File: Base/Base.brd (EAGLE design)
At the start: 83.8 x 61 mm, 25 parts

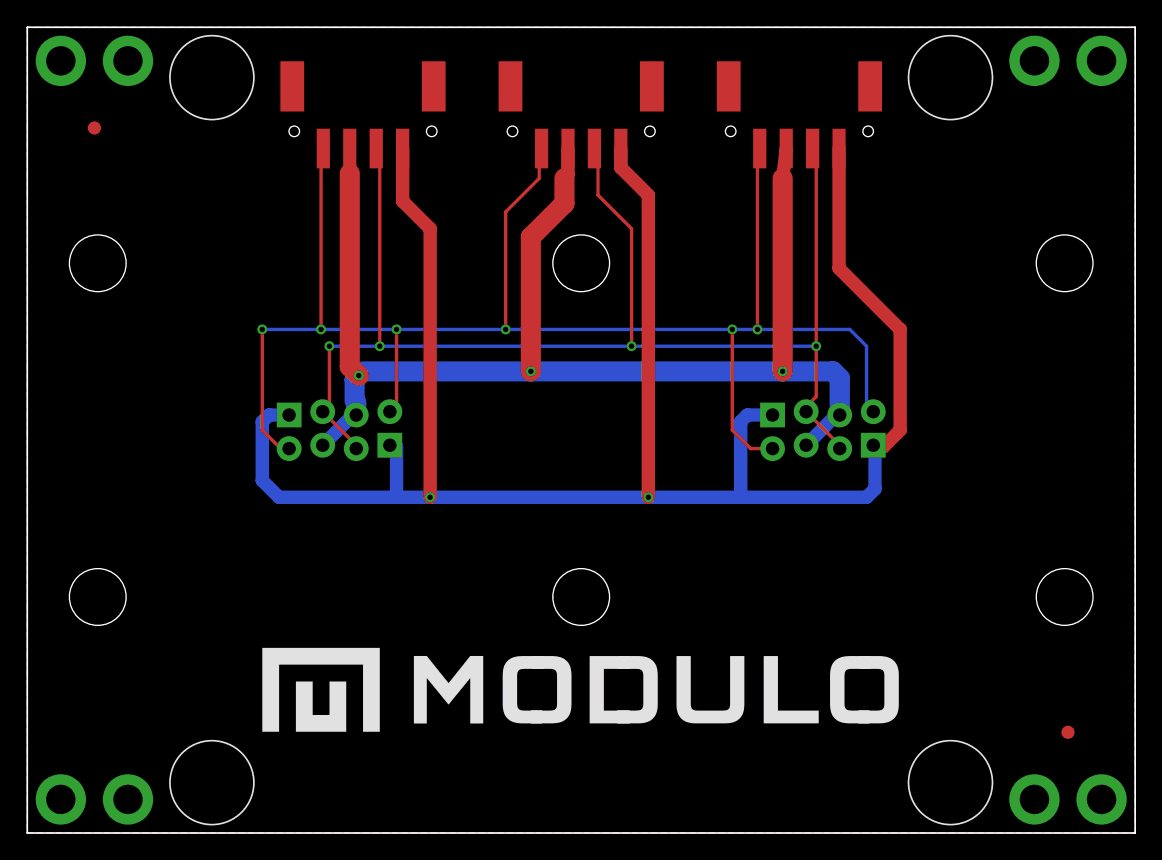
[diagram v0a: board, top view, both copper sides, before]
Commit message: Check point of current PCB designs. Among other things I think this change includes rewiring of programming lines on many of the boards,.
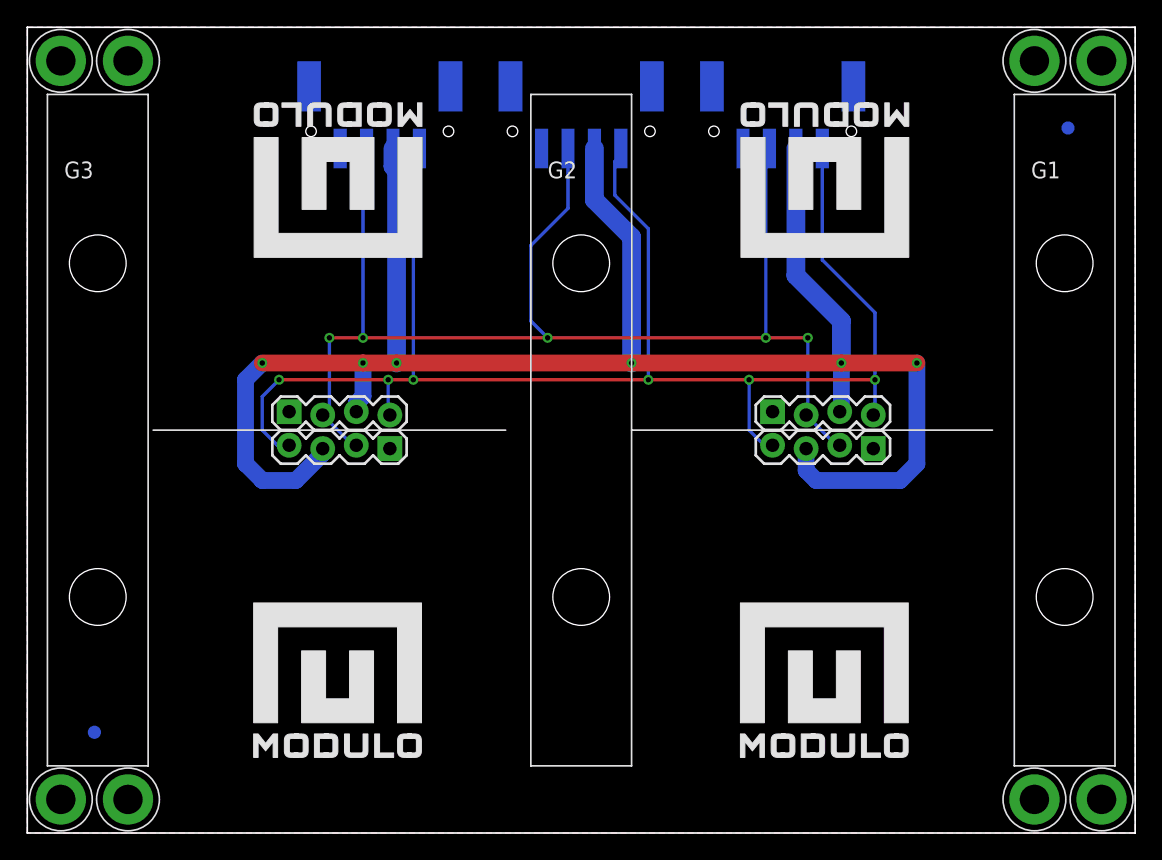
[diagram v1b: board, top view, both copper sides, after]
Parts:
- moved H1 78.7 mm to (2.54, 58.4), flipped to the top
- moved H5 78.7 mm to (2.54, 2.54), flipped to the top
- moved H6 78.7 mm to (81.3, 2.54), flipped to the top
- moved H8 78.7 mm to (81.3, 58.4), flipped to the top
- moved F1 73.7 mm to (5.08, 7.62), flipped to the bottom
- moved F2 73.7 mm to (78.7, 53.3), flipped to the bottom
- moved G1 73.2 mm to (78.5, 30.5), flipped to the top
- moved G3 73.2 mm to (5.33, 30.5), flipped to the top
- moved H2 68.6 mm to (7.62, 2.54), flipped to the top
- moved H3 68.6 mm to (76.2, 58.4), flipped to the top
- moved H4 68.6 mm to (76.2, 2.54), flipped to the top
- moved H7 68.6 mm to (7.62, 58.4), flipped to the top
- moved U$1 47.6 mm to (65.4, 12.1), flipped to the bottom
- moved JP1 44.3 mm to (19.8, 31.8), flipped to the top
- moved JP6 44.3 mm to (64.0, 29.2), flipped to the top
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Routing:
- net GND: track 150.2 -> 0.00 mm, vias 2 -> 0
- net VCC: track 102.0 -> 142.8 mm, vias 3 -> 6
- net SCL: track 124.9 -> 119.0 mm
- net SDA: track 104.9 -> 100.2 mm, vias 4 -> 5

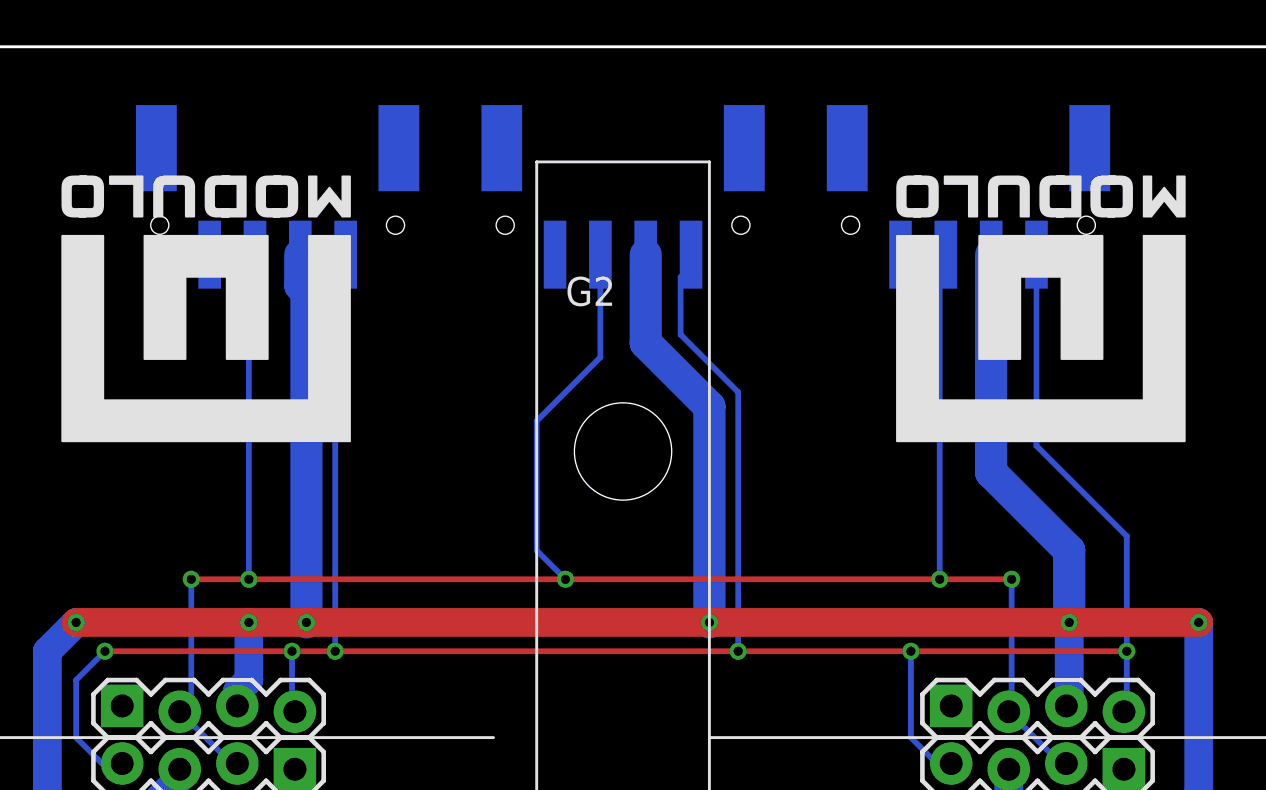
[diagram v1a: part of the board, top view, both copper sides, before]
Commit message: Updated to grove compatible connector footprints
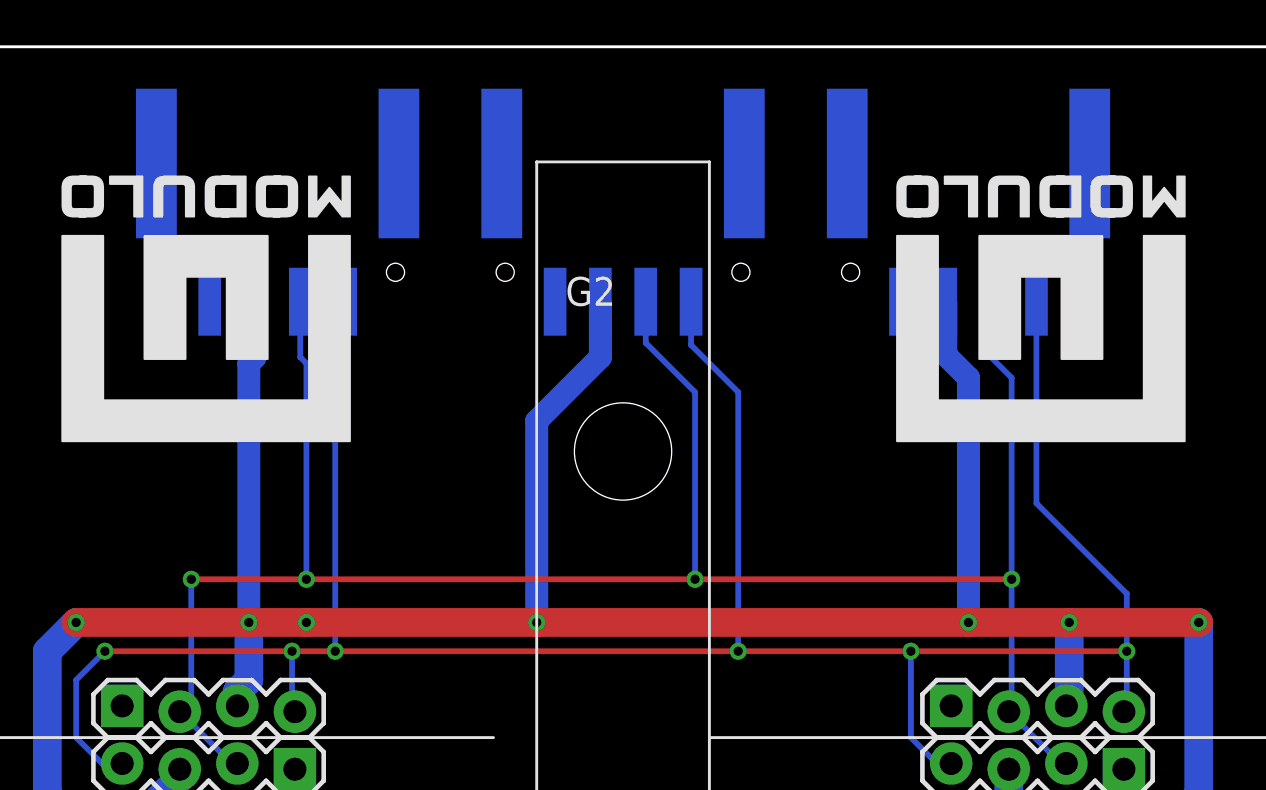
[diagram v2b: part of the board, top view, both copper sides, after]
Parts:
- JP2, JP4, JP7: value HEADER-1X4-JST-PA-SIDE-SMD -> HEADER-MODULO
- moved JP2 15.2 mm to (26.7, 61.0)
- moved JP4 15.2 mm to (41.9, 61.0)
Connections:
- net SDA: now also JP2.3, JP4.3, JP7.3; no longer JP2.2, JP4.2, JP7.2
- net VCC: now also JP2.2, JP4.2, JP7.2; no longer JP2.3, JP4.3, JP7.3
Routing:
- net VCC: track 142.8 -> 135.5 mm, vias 6 -> 7
- net SDA: track 100.2 -> 93.5 mm, vias 5 -> 4
- net SCL: track 119.0 -> 112.4 mm

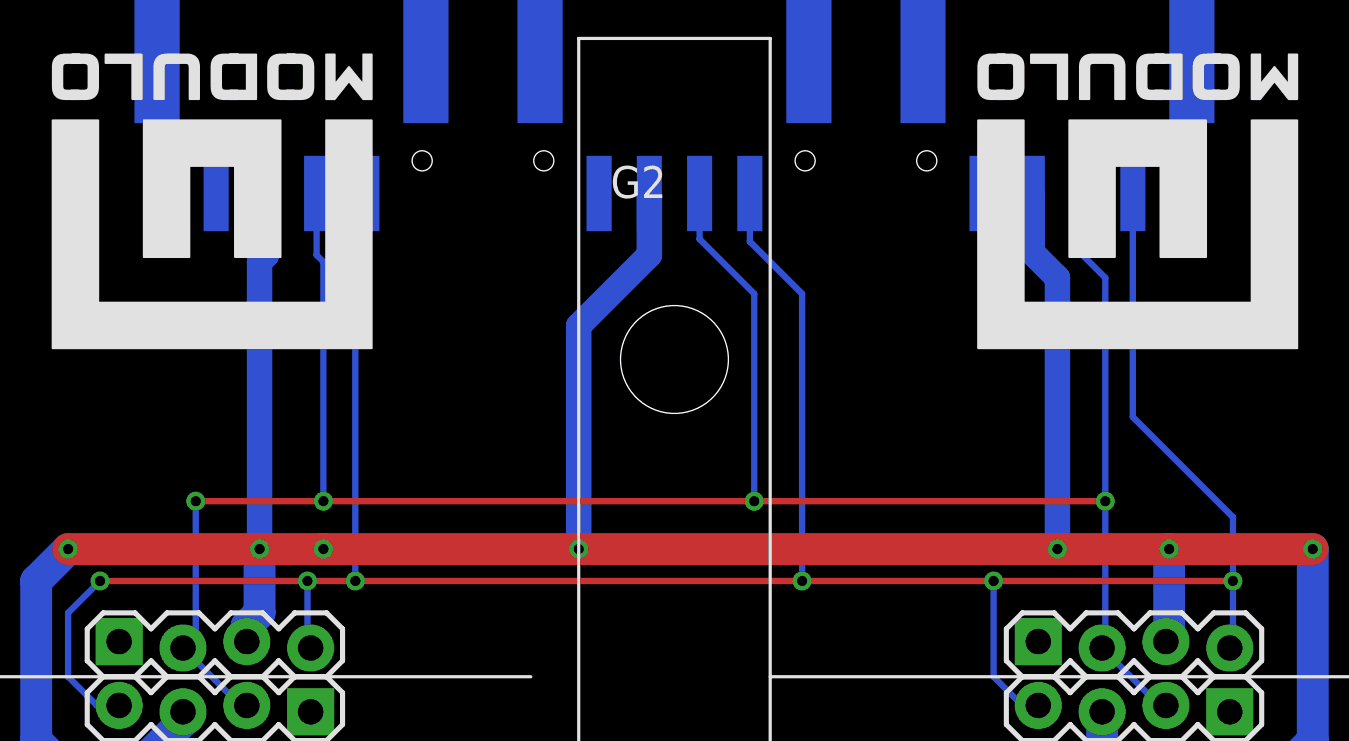
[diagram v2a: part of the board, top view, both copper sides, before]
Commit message: Tented vias Updated extension cable connectors Added 3.3v regulator and clamping diodes
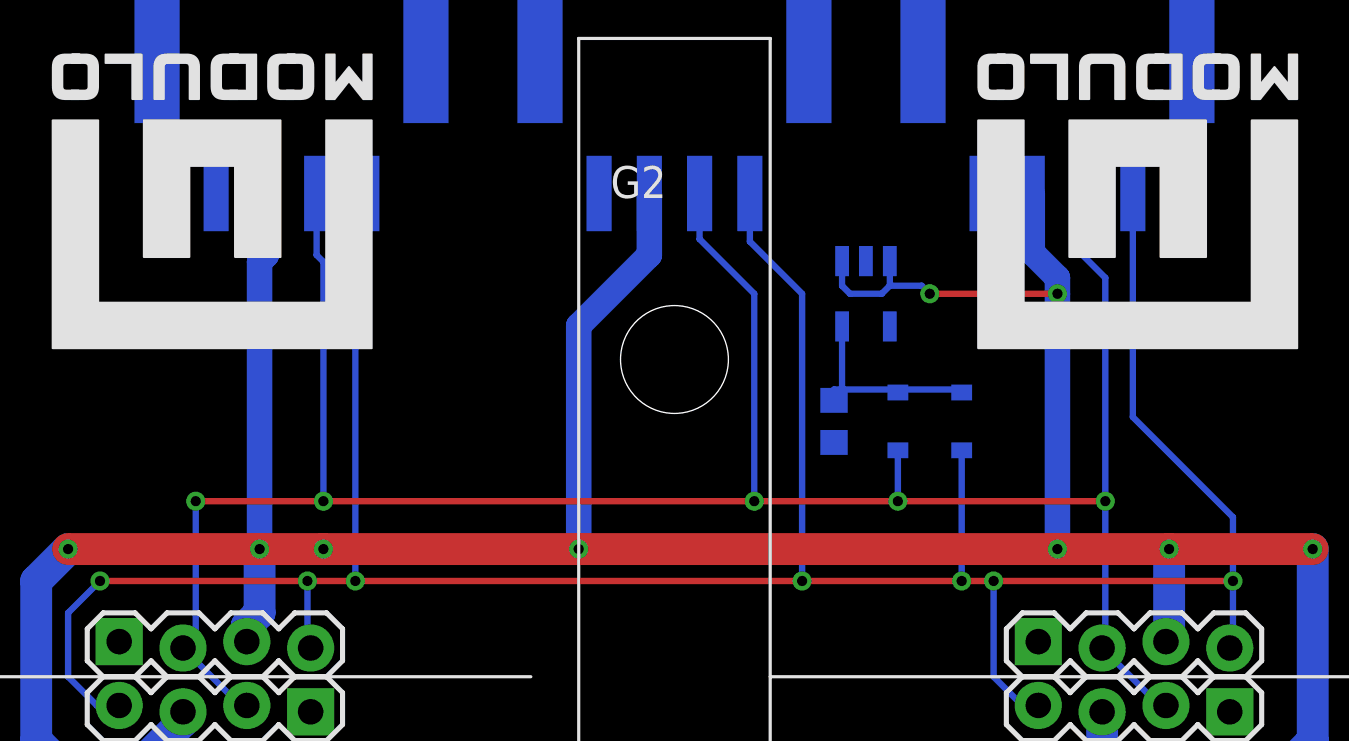
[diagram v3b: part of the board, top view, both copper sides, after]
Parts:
- added C1: 10uF, Modulo:0603
- added D1, D2: RB751V40, Modulo:SOD-323
- added U1: VREG-MIC5205-3.3V, Modulo:SOT23-5
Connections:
- new net 3.3V: C1.1, D1.C, D2.C, U1.5
- net GND: now also C1.2, U1.2
- net SCL: now also D2.A
- net SDA: now also D1.A
- net VCC: now also U1.1, U1.3
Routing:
- net VCC: track 135.5 -> 146.5 mm, vias 7 -> 9
- net 3.3V: track 0.00 -> 8.81 mm
- net SCL: track 112.4 -> 117.6 mm, vias 6 -> 7
- net SDA: track 93.5 -> 95.5 mm, vias 4 -> 5
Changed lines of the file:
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@@
 </class>
 </classes>
-<designrules name="LaenPCBOrder">
+<designrules name="Modulo">
 <description language="de">&lt;b&gt;EAGLE Design Rules&lt;/b&gt;
 &lt;p&gt;
@@
 Einstellungen hier und speichern die Design Rules unter
 einem neuen Namen ab.</description>
-<description language="en">&lt;b&gt;Laen's PCB Order Design Rules&lt;/b&gt;
-&lt;p&gt;
-Please make sure your boards conform to these design rules.</description>
+<description language="en">&lt;b&gt;Modulo Design Rules&lt;/b&gt;
+</description>
 <param name="layerSetup" value="(1*16)"/>
 <param name="mtCopper" value="0.0356mm 0.0356mm 0.0356mm 0.0356mm 0.0356mm 0.0356mm 0.0356mm 0.0356mm 0.0356mm 0.0356mm 0.0356mm 0.0356mm 0.0356mm 0.0356mm 0.0356mm 0.0356mm"/>
@@
 <param name="mlMinCreamFrame" value="0mil"/>
 <param name="mlMaxCreamFrame" value="0mil"/>
-<param name="mlViaStopLimit" value="0mil"/>
+<param name="mlViaStopLimit" value="25mil"/>
 <param name="srRoundness" value="0"/>
 <param name="srMinRoundness" value="0mil"/>
@@
 <element name="U$5" library="Modulo" package="LOGO-0.5" value="" x="60.325" y="55.245" rot="R180"/>
 <element name="U$6" library="Modulo" package="LOGO-0.5" value="" x="23.495" y="55.245" rot="R180"/>
-<element name="JP2" library="Modulo" package="JST-PA-SIDE-SMD" value="HEADER-MODULO" x="26.67" y="60.96" rot="MR180"/>
-<element name="JP4" library="Modulo" package="JST-PA-SIDE-SMD" value="HEADER-MODULO" x="41.91" y="60.96" rot="MR180"/>
-<element name="JP7" library="Modulo" package="JST-PA-SIDE-SMD" value="HEADER-MODULO" x="57.15" y="60.96" rot="MR180"/>
+<element name="JP2" library="Modulo" package="JST-PA-SIDE-SMD" value="HEADER-MODULO" x="26.67" y="60.96" rot="MR180">
+<attribute name="PARTNUM" value="4P-SMD-2.0-90D" x="26.67" y="60.96" size="1.778" layer="28" rot="MR180" display="off"/>
+</element>
+<element name="JP4" library="Modulo" package="JST-PA-SIDE-SMD" value="HEADER-MODULO" x="41.91" y="60.96" rot="MR180">
+<attribute name="PARTNUM" value="4P-SMD-2.0-90D" x="41.91" y="60.96" size="1.778" layer="28" rot="MR180" display="off"/>
+</element>
+<element name="JP7" library="Modulo" package="JST-PA-SIDE-SMD" value="HEADER-MODULO" x="57.15" y="60.96" rot="MR180">
+<attribute name="PARTNUM" value="4P-SMD-2.0-90D" x="57.15" y="60.96" size="1.778" layer="28" rot="MR180" display="off"/>
+</element>
+<element name="D1" library="Modulo" package="SOD-323" value="RB751V40" x="50.8" y="40.64" smashed="yes" rot="MR270">
+<attribute name="PARTNUM" value="RB751V40" x="50.8" y="40.64" size="1.778" layer="28" rot="MR270" display="off"/>
+<attribute name="NAME" x="50.546" y="38.354" size="0.4064" layer="26" rot="MR180"/>
+</element>
+<element name="D2" library="Modulo" package="SOD-323" value="RB751V40" x="53.34" y="40.64" smashed="yes" rot="MR270">
+<attribute name="PARTNUM" value="RB751V40" x="53.34" y="40.64" size="1.778" layer="28" rot="MR270" display="off"/>
+<attribute name="NAME" x="53.086" y="38.354" size="0.4064" layer="26" rot="MR180"/>
+</element>
+<element name="U1" library="Modulo" package="SOT23-5" value="VREG-MIC5205-3.3V" x="49.53" y="45.72" rot="MR180">
+<attribute name="PARTNUM" value="MIC5205-3.3YM5 TR" x="49.53" y="45.72" size="1.778" layer="28" rot="MR180" display="off"/>
+</element>
+<element name="C1" library="Modulo" package="0603" value="10uF" x="48.26" y="40.64" smashed="yes" rot="MR270">
+<attribute name="PARTNUM" value="GRM188R61C106MA73D" x="48.26" y="40.64" size="1.778" layer="28" rot="MR270" display="off"/>
+<attribute name="NAME" x="47.8155" y="38.70325" size="0.508" layer="26" font="vector" rot="MR180"/>
+<attribute name="VALUE" x="47.244" y="38.06825" size="0.508" layer="28" font="vector" rot="MR180"/>
+</element>
 </elements>
 <signals>
@@
 <wire x1="56.15" y1="49.71" x2="56.15" y2="47.355" width="1.016" layer="16"/>
 <wire x1="56.15" y1="47.355" x2="57.15" y2="46.355" width="1.016" layer="16"/>
-<wire x1="57.15" y1="46.355" x2="57.15" y2="35.56" width="1.016" layer="16"/>
 <via x="57.15" y="35.56" extent="1-16" drill="0.4064"/>
+<contactref element="U1" pad="1"/>
+<contactref element="U1" pad="3"/>
+<wire x1="57.15" y1="46.355" x2="57.15" y2="45.72" width="1.016" layer="16"/>
+<wire x1="57.15" y1="45.72" x2="57.15" y2="35.56" width="1.016" layer="16"/>
+<wire x1="50.48" y1="47.0201" x2="50.48" y2="46.04" width="0.254" layer="16"/>
+<wire x1="48.58" y1="47.0201" x2="48.58" y2="46.035" width="0.254" layer="16"/>
+<wire x1="48.58" y1="46.035" x2="48.895" y2="45.72" width="0.254" layer="16"/>
+<wire x1="48.895" y1="45.72" x2="50.16" y2="45.72" width="0.254" layer="16"/>
+<wire x1="50.16" y1="45.72" x2="50.48" y2="46.04" width="0.254" layer="16"/>
+<wire x1="50.48" y1="46.04" x2="51.75" y2="46.04" width="0.254" layer="16"/>
+<wire x1="51.75" y1="46.04" x2="52.07" y2="45.72" width="0.254" layer="16"/>
+<via x="52.07" y="45.72" extent="1-16" drill="0.4064"/>
+<wire x1="52.07" y1="45.72" x2="57.15" y2="45.72" width="0.254" layer="1"/>
+<via x="57.15" y="45.72" extent="1-16" drill="0.4064"/>
 </signal>
 <signal name="SDA">
@@
 <wire x1="22.86" y1="37.465" x2="27.94" y2="37.465" width="0.254" layer="1"/>
 <wire x1="27.94" y1="37.465" x2="45.085" y2="37.465" width="0.254" layer="1"/>
-<wire x1="45.085" y1="37.465" x2="59.055" y2="37.465" width="0.254" layer="1"/>
+<wire x1="45.085" y1="37.465" x2="50.8" y2="37.465" width="0.254" layer="1"/>
+<wire x1="50.8" y1="37.465" x2="59.055" y2="37.465" width="0.254" layer="1"/>
 <wire x1="59.055" y1="37.465" x2="59.055" y2="31.75" width="0.254" layer="16"/>
 <wire x1="59.055" y1="31.75" x2="58.928" y2="31.623" width="0.254" layer="16"/>
@@
 <wire x1="45.085" y1="45.72" x2="45.085" y2="37.465" width="0.254" layer="16"/>
 <via x="45.085" y="37.465" extent="1-16" drill="0.4064"/>
+<contactref element="D1" pad="A"/>
+<wire x1="50.8" y1="39.49" x2="50.8" y2="37.465" width="0.254" layer="16"/>
+<via x="50.8" y="37.465" extent="1-16" drill="0.4064"/>
 </signal>
 <signal name="SCL">
@@
 <wire x1="46.99" y1="45.72" x2="46.99" y2="34.29" width="0.254" layer="16"/>
 <via x="46.99" y="34.29" extent="1-16" drill="0.4064"/>
-<wire x1="46.99" y1="34.29" x2="54.61" y2="34.29" width="0.254" layer="1"/>
+<wire x1="46.99" y1="34.29" x2="53.34" y2="34.29" width="0.254" layer="1"/>
 <via x="29.21" y="34.29" extent="1-16" drill="0.4064"/>
+<wire x1="53.34" y1="34.29" x2="54.61" y2="34.29" width="0.254" layer="1"/>
 <wire x1="29.21" y1="34.29" x2="27.305" y2="34.29" width="0.254" layer="1"/>
 <wire x1="29.21" y1="34.29" x2="46.99" y2="34.29" width="0.254" layer="1"/>
@@
 <wire x1="60.15" y1="40.815" x2="64.135" y2="36.83" width="0.254" layer="16"/>
 <wire x1="64.135" y1="36.83" x2="64.135" y2="34.29" width="0.254" layer="16"/>
+<contactref element="D2" pad="A"/>
+<wire x1="53.34" y1="39.49" x2="53.34" y2="34.29" width="0.254" layer="16"/>
+<via x="53.34" y="34.29" extent="1-16" drill="0.4064"/>
 </signal>
 <signal name="GND">
@@
 <contactref element="JP4" pad="1"/>
 <contactref element="JP7" pad="1"/>
+<contactref element="U1" pad="2"/>
+<contactref element="C1" pad="2"/>
+</signal>
+<signal name="3.3V">
+<contactref element="C1" pad="1"/>
+<contactref element="U1" pad="5"/>
+<contactref element="D1" pad="C"/>
+<contactref element="D2" pad="C"/>
+<wire x1="48.26" y1="41.4782" x2="48.26" y2="41.91" width="0.254" layer="16"/>
+<wire x1="48.26" y1="41.91" x2="50.68" y2="41.91" width="0.254" layer="16"/>
+<wire x1="50.68" y1="41.91" x2="50.8" y2="41.79" width="0.254" layer="16"/>
+<wire x1="53.34" y1="41.79" x2="53.34" y2="41.91" width="0.254" layer="16"/>
+<wire x1="53.34" y1="41.91" x2="50.92" y2="41.91" width="0.254" layer="16"/>
+<wire x1="50.92" y1="41.91" x2="50.8" y2="41.79" width="0.254" layer="16"/>
+<wire x1="48.58" y1="44.4199" x2="48.58" y2="41.7982" width="0.254" layer="16"/>
+<wire x1="48.58" y1="41.7982" x2="48.26" y2="41.4782" width="0.254" layer="16"/>
 </signal>
 </signals>
